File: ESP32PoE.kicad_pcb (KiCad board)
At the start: 4 copper layers, 90 x 40 mm, 56 parts, among them J1 Conn_01x20_Pin, J2 Conn_01x20_Pin, J3 Conn_01x04_Pin, SW1 SW_Push, SW2 SW_Push, U1 W5500, U2 MagJack-A70-112-331N126, U3 AMS1117-3.3, U4 ESP32-S3-WROOM-1, U7 AG9905LP, Y1 XO32F025000GEHE001

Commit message: feat: improve silkscreen
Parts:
- added G***: LOGO, ESP32PoE:Arrow, F.Cu at (156.7, 74.1)
- added G***: LOGO, ESP32PoE:Arrow, B.Cu at (119.3, 69.2)
- moved C15 0.55 mm to (133.2, 88.3)
- moved C11 0.50 mm to (114.5, 81.6)
- moved C16 0.50 mm to (133.4, 90.1)
- moved C20 0.45 mm to (133.2, 91.8)
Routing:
- net Net-(C11-Pad1): track 6.30 -> 6.80 mm
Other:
- board text added: "LAN"
- board text added: "PoE"

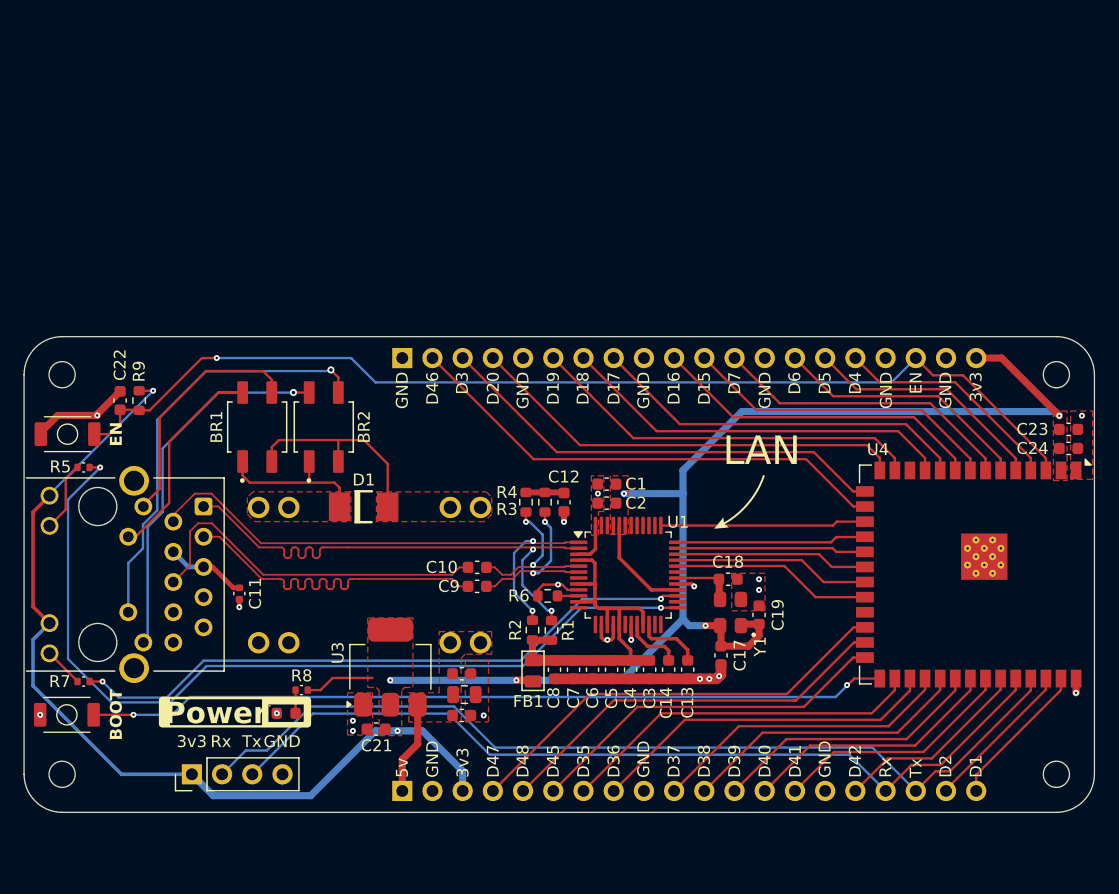
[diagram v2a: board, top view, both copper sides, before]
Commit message: feat: redesign to smaller form factor
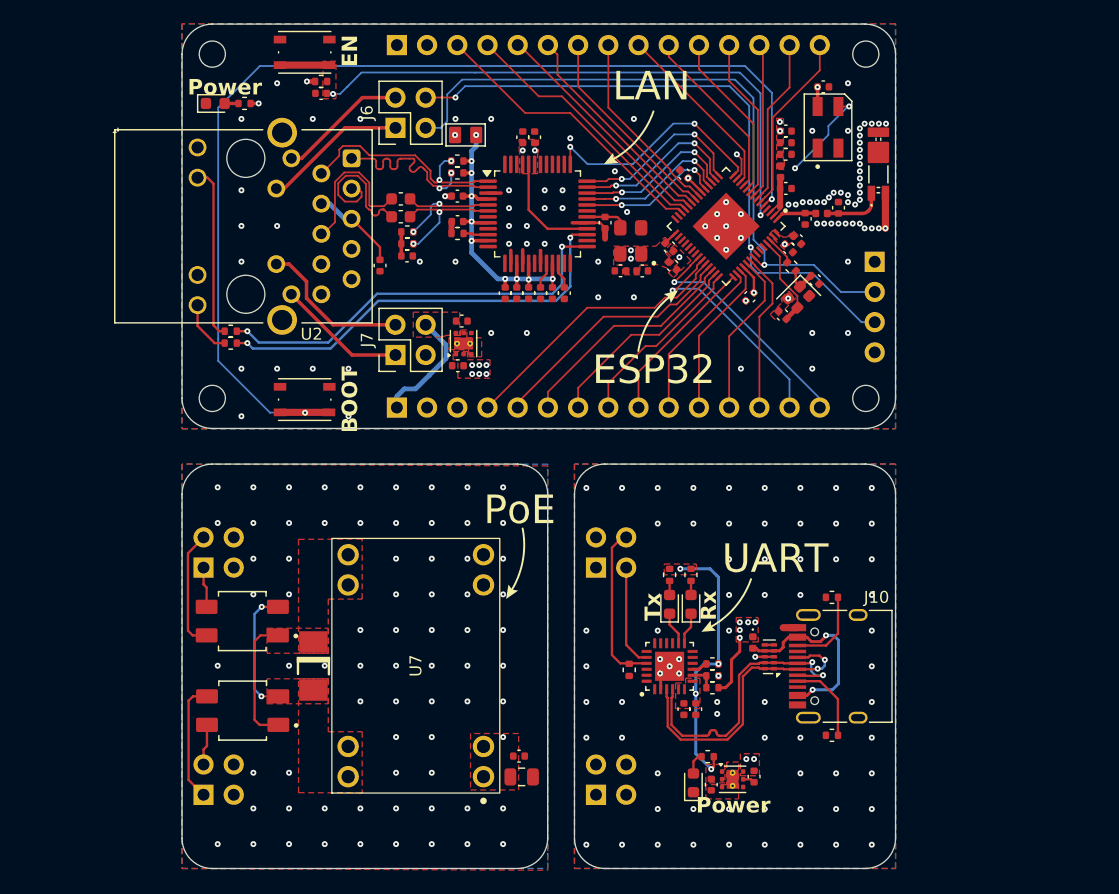
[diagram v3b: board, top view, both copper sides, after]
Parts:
- added AE1: Ant_RFECA3216060A1T_1206, Hardware Components:Ant_RFECA3216060A1T, F.Cu at (168.3, 46.3)
- added C25: 2p7, Hardware Components:C_0402_1005Metric, F.Cu at (162.1, 50.1)
- added C26: 2p4, Hardware Components:C_0402_1005Metric, F.Cu at (164.9, 49.2)
- added C27: 100n, Hardware Components:C_0402_1005Metric, F.Cu at (160.5, 44.7)
- added C28: 100n, Hardware Components:C_0402_1005Metric, F.Cu at (160.5, 47.5)
- added C29: 100n, Hardware Components:C_0402_1005Metric, F.Cu at (151.9, 46.3)
- added C30: 100n, Hardware Components:C_0402_1005Metric, F.Cu at (157.4, 56.6)
- added C31: 1u, Hardware Components:C_0402_1005Metric, F.Cu at (160.5, 43.7)
- added C32: 10u, Hardware Components:C_0402_1005Metric, F.Cu at (160.5, 42.7)
- added C33: 100n, Hardware Components:C_0402_1005Metric, F.Cu at (160.7, 52.6)
- added C34: 1u, Hardware Components:C_0402_1005Metric, F.Cu at (161.4, 51.9)
- added C35: 1u, Hardware Components:C_0402_1005Metric, F.Cu at (150.9, 54.0)
- added C36: 100n, Hardware Components:C_0402_1005Metric, F.Cu at (150.7, 52.5)
- added C37: 100n, Hardware Components:C_0402_1005Metric, F.Cu at (152.9, 91.3)
- added C38: 4u7, Hardware Components:C_0402_1005Metric, F.Cu at (151.9, 91.3)
- added C39: 1u, Hardware Components:C_0402_1005Metric, F.Cu at (157.8, 97.0)
- added C40: 1u, Hardware Components:C_0402_1005Metric, F.Cu at (154.2, 97.7)
- added C41: 100n, Hardware Components:C_0402_1005Metric, F.Cu at (163.6, 39.0)
- added D2: LED, Hardware Components:LED_0603_1608Metric, F.Cu at (152.7, 97.5)
- added D4: D_Schottky_Small, Hardware Components:D_0402_1005Metric, F.Cu at (157.7, 85.7)
- added D5: LED, Hardware Components:LED_0603_1608Metric, F.Cu at (150.7, 82.5)
- added D6: LED, Hardware Components:LED_0603_1608Metric, F.Cu at (152.5, 82.5)
- added D7: SK6812MINI, Hardware Components:LED_SK6812MINI, F.Cu at (164.0, 42.4)
- added G***: LOGO, ESP32PoE:Arrow, F.Cu at (155.6, 82.8)
- added G***: LOGO, ESP32PoE:Arrow, F.Cu at (149.6, 58.5)
- added J10: USB_C_Receptacle_USB2.0_16P, Hardware Components:USB_C_Receptacle_HRO_TYPE-C-31-M-12, F.Cu at (165.5, 87.7)
- added J4: Conn_02x02_Counter_Clockwise, Connector_PinSocket_2.54mm:PinSocket_2x02_P2.54mm_Vertical, B.Cu at (111.5, 79.4)
- added J5: Conn_02x02_Counter_Clockwise, Connector_PinSocket_2.54mm:PinSocket_2x02_P2.54mm_Vertical, B.Cu at (111.5, 98.5)
- added J6: Conn_02x02_Counter_Clockwise, Hardware Components:Conn_PinHeader_2x02_P2.54mm_Vertical, F.Cu at (127.6, 42.4)
- added J7: Conn_02x02_Counter_Clockwise, Hardware Components:Conn_PinHeader_2x02_P2.54mm_Vertical, F.Cu at (127.6, 61.5)
- added J8: Conn_02x02_Counter_Clockwise, Connector_PinSocket_2.54mm:PinSocket_2x02_P2.54mm_Vertical, B.Cu at (144.5, 79.4)
- added J9: Conn_02x02_Counter_Clockwise, Connector_PinSocket_2.54mm:PinSocket_2x02_P2.54mm_Vertical, B.Cu at (144.5, 98.5)
- added L1: 2.4nH, Hardware Components:L_0402_1005Metric, F.Cu at (163.5, 49.6)
- added L2: 2u, Hardware Components:L_0402_1005Metric, F.Cu at (160.0, 46.1)
- added R10: 22, Hardware Components:R_0402_1005Metric, F.Cu at (160.9, 54.1)
- added R11: 1k, Hardware Components:R_0402_1005Metric, F.Cu at (150.7, 80.0)
- added R12: 10k, Hardware Components:R_0402_1005Metric, F.Cu at (147.3, 88.0)
- added R13: 5k1, Hardware Components:R_0402_1005Metric, F.Cu at (164.3, 93.5)
- added R14: 5k1, Hardware Components:R_0402_1005Metric, F.Cu at (164.3, 81.9)
- added R15: 1k, Hardware Components:R_0402_1005Metric, F.Cu at (154.3, 87.5)
- added R16: 22k1, Hardware Components:R_0402_1005Metric, F.Cu at (154.3, 89.5)
- added R17: 47k5, Hardware Components:R_0402_1005Metric, F.Cu at (154.3, 88.5)
- added R18: 1k, Hardware Components:R_0402_1005Metric, F.Cu at (152.5, 80.0)
- added R19: 1k, Hardware Components:R_0402_1005Metric, F.Cu at (153.9, 95.3)
- added U13: TPD4EUSB30, Hardware Components:TPD4EUSB30_USON-10, F.Cu at (159.1, 86.9)
- added U5: ESP32-S3FN8, Hardware Components:MCU_ESP32-S3FN8, F.Cu at (155.4, 50.7)
- added U6: CP2102N-A02-GQFN24R, Hardware Components:CP2102-A02-GQ-QFN-50P, F.Cu at (150.7, 87.7)
- added Y2: ECS-400-10-37B2-CKM-TR, Hardware Components:Oscillator_ECS_400-10-37B2-CKM-TR, F.Cu at (161.5, 56.7)
- BR1, BR2: footprint ESP32PoE:CDBHM1100L-G -> Hardware Components:MB110S
- C1, C13, C14, C15, C17, C18, C19, C2, C22, C3, C4, C5, C6, C7, C8: footprint Capacitor_SMD:C_0603_1608Metric -> Hardware Components:C_0402_1005Metric
- C10, C9: footprint Capacitor_SMD:C_0603_1608Metric -> Hardware Components:C_0603_1608Metric
- C11: footprint Capacitor_SMD:C_0402_1005Metric -> Hardware Components:C_0402_1005Metric
- C12: value 22n -> 10n; footprint Capacitor_SMD:C_0603_1608Metric -> Hardware Components:C_0402_1005Metric
- C16: footprint Capacitor_SMD:C_0805_2012Metric -> Hardware Components:C_0805_2012Metric
- C20, C21: value 22u -> 1u; footprint Capacitor_SMD:C_0603_1608Metric -> Hardware Components:C_0402_1005Metric
- C23: value 10u -> 12pF; footprint Capacitor_SMD:C_0603_1608Metric -> Hardware Components:C_0402_1005Metric
- C24: value 100n -> 12pF; footprint Capacitor_SMD:C_0603_1608Metric -> Hardware Components:C_0402_1005Metric
- D1: footprint ESP32PoE:SMAJ58A -> Hardware Components:D_SMAJ58A
- D3: footprint LED_SMD:LED_0603_1608Metric -> Hardware Components:LED_0603_1608Metric
- G***: moved to F.Cu
- J1, J2: value Conn_01x20_Pin -> Conn_01x15_Pin; footprint Connector_PinHeader_2.54mm:PinHeader_1x20_P2.54mm_Vertical -> Connector_PinHeader_2.54mm:PinHeader_1x15_P2.54mm_Vertical
- J3: moved to B.Cu
- R1, R2, R3, R4, R6, R9: footprint Resistor_SMD:R_0603_1608Metric -> Hardware Components:R_0402_1005Metric
- R5, R7, R8: footprint Resistor_SMD:R_0402_1005Metric -> Hardware Components:R_0402_1005Metric
- SW1, SW2: footprint ESP32PoE:SMD,3x4mm -> Hardware Components:SW_PTS815SJM250SMTRLFS
- U1: footprint Package_QFP:LQFP-48_7x7mm_P0.5mm -> Hardware Components:LQFP-48_7x7mm_P0.5mm
- U2: footprint ESP32PoE:TRJG0926HENL -> Hardware Components:RJ45_USAKRO_DGUK111Q334AB2A2DP057
- U3: value AMS1117-3.3 -> TLV76733DRVx; footprint Package_TO_SOT_SMD:SOT-223-3_TabPin2 -> Hardware Components:WSON-6-1EP_2x2mm_P0.65mm_EP1x1.6mm_ThermalVias
- U4: value ESP32-S3-WROOM-1 -> TLV76733DRVx; footprint RF_Module:ESP32-S3-WROOM-1 -> Hardware Components:WSON-6-1EP_2x2mm_P0.65mm_EP1x1.6mm_ThermalVias
- U7: footprint ESP32PoE:AG9905LP -> Hardware Components:POE_AG9905LP; moved to F.Cu
- Y1: footprint ESP32PoE:SMD3225-4P -> Hardware Components:Oscillator_TDK_SMD3225-4P
- moved J3 71.8 mm to (167.9, 53.7), turned to 180 degrees
- moved H4 62.6 mm to (167.2, 36.2), turned to 90 degrees
- moved H2 61.9 mm to (112.2, 36.2)
- moved SS3 51.7 mm to (164.2, 42.6)
- moved D3 51.6 mm to (112.5, 40.4)
- moved U4 50.2 mm to (133.4, 60.6), turned to 90 degrees
- moved R8 49.6 mm to (114.9, 40.4)
- moved FB1 45.4 mm to (133.5, 43.0), turned to 0 degrees
- moved C7 41.0 mm to (132.8, 48.2), turned to 180 degrees
- moved R2 39.9 mm to (132.8, 45.2), turned to 180 degrees
- moved C6 39.3 mm to (132.8, 50.3), turned to 180 degrees
- moved R1 39.3 mm to (132.8, 46.2), turned to 180 degrees
- moved SW1 37.8 mm to (120.0, 36.1)
- moved G*** 33.7 mm to (156.5, 50.7)
- moved C14 33.4 mm to (139.8, 56.3)
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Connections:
- BR1 pad 3: /LAN/VINA -> /PoE/VINB
- BR1 pad 4: /LAN/VINB -> /PoE/VINA
- BR2 pad 3: /LAN/VINC -> /PoE/VIND
- BR2 pad 4: /LAN/VIND -> /PoE/VINC
- C15 pad 1: GND -> GND_PoE
- C15 pad 2: +5V -> +5V_PoE
- C16 pad 1: +5V -> +5V_PoE
- C16 pad 2: GND -> GND_PoE
- C22 pad 1: /ESP/EN -> /MCU/EN
- C23 pad 1: +3.3V -> Net-(C23-Pad1)
- C24 pad 1: +3.3V -> /MCU/XTAL_N
- J1 pad 10: /ESP/IO37 -> /MCU/IO39
- J1 pad 11: /ESP/IO38 -> /MCU/IO40
- J1 pad 12: /ESP/IO39 -> /MCU/IO41
- J1 pad 13: /ESP/IO40 -> /MCU/IO42
- J1 pad 14: /ESP/IO41 -> /MCU/IO47
- J1 pad 15: GND -> /MCU/IO48
- J1 pad 4: /ESP/IO47 -> /MCU/IO33
- J1 pad 5: /ESP/IO48 -> /MCU/IO34
- J1 pad 6: /ESP/IO45 -> /MCU/IO35
- J1 pad 7: /ESP/IO35 -> /MCU/IO36
- J1 pad 8: /ESP/IO36 -> /MCU/IO37
- J1 pad 9: GND -> /MCU/IO38
- J2 pad 1: GND -> +3.3V
- J2 pad 10: /ESP/IO16 -> /MCU/IO6
- J2 pad 11: /ESP/IO15 -> /MCU/IO5
- J2 pad 12: /ESP/IO7 -> /MCU/IO4
- J2 pad 13: GND -> /MCU/IO3
- J2 pad 14: /ESP/IO6 -> /MCU/IO2
- J2 pad 15: /ESP/IO5 -> /MCU/IO1
- J2 pad 2: /ESP/IO46 -> GND
- J2 pad 3: /ESP/IO3 -> /MCU/IO20
- J2 pad 4: /ESP/IO20 -> /MCU/IO19
- J2 pad 5: GND -> /MCU/IO18
- J2 pad 6: /ESP/IO19 -> /MCU/IO17
- J2 pad 7: /ESP/IO18 -> /MCU/IO16
- J2 pad 8: /ESP/IO17 -> /MCU/IO15
- J2 pad 9: GND -> /MCU/IO7
- J3 pad 2: /ESP/TX -> TX
- J3 pad 3: /ESP/RX -> RX
- R9 pad 2: /ESP/EN -> /MCU/EN
- SW1 pad 2: /ESP/EN -> /MCU/EN
- SW2 pad 2: /ESP/BOOT_OPT -> /MCU/BOOT_OPT
- U1 pad 32: /ESP/LAN.~{SCS} -> /LAN/LAN.~{SCS}
- U1 pad 33: /ESP/LAN.SCLK -> /LAN/LAN.SCLK
- U1 pad 34: /ESP/LAN.MISO -> /LAN/LAN.MISO
- U1 pad 35: /ESP/LAN.MOSI -> /LAN/LAN.MOSI
- U1 pad 36: /ESP/LAN.~{INT} -> /LAN/LAN.~{INT}
- U1 pad 37: /ESP/LAN.~{RST} -> /LAN/LAN.~{RST}
- U3 pad 1: GND -> +3.3V_USB
- U3 pad 2: +3.3V -> +3.3V_USB
- U3 pad 3: +5V -> GND_USB
- U4 pad 1: GND -> +3.3V
- U4 pad 3: /ESP/EN -> GND
- U4 pad 4: /ESP/IO4 -> unconnected-(U4-EN-Pad4)
- U4 pad 5: /ESP/IO5 -> GND
- U4 pad 6: /ESP/IO6 -> +5V
- U4 pad 7: /ESP/IO7 -> GND
- U7 pad 1: +5V -> +5V_PoE
- U7 pad 2: GND -> GND_PoE
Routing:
- net +3.3V: track 191.1 -> 17.9 mm, vias 7 -> 19
- net /MCU/BOOT_OPT: track 0.00 -> 93.3 mm, vias 0 -> 2
- net /ESP/EN: track 89.5 -> 0.00 mm, vias 1 -> 0
- net /ESP/TX: track 77.8 -> 0.00 mm
- net /ESP/RX: track 73.5 -> 0.00 mm
- net /ESP/BOOT_OPT: track 67.4 -> 0.00 mm, vias 2 -> 0
- net TX: track 0.00 -> 57.0 mm, vias 0 -> 1
- net RX: track 0.00 -> 55.0 mm, vias 0 -> 2
- net /MCU/EN: track 0.00 -> 52.7 mm, vias 0 -> 2
- net /ESP/IO46: track 41.5 -> 0.00 mm
- net /LAN/ETH.LEDG: track 74.2 -> 35.0 mm
- net /ESP/IO3: track 38.5 -> 0.00 mm
- net /ESP/IO20: track 37.1 -> 0.00 mm
- net /ESP/IO47: track 37.0 -> 0.00 mm
- net /ESP/IO48: track 33.9 -> 0.00 mm
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- added copper zone on In2.Cu, net +3.3V
- added copper zone on F.Cu, net +3.3V_USB
- added copper zone on B.Cu, net +5V_PoE
- added copper zone on F.Cu, net +5V_PoE
- added copper zone on F.Cu, net +5V_USB
- added copper zone on In2.Cu, net +5V_USB
- added copper zone on F.Cu, net /MCU/EN
- added copper zone on F.Cu, net /MCU/RF_ANT
- added copper zone on B.Cu, net GND
- added copper zone on F.Cu, net GND_PoE
- added copper zone on In1.Cu, net GND_PoE
- added copper zone on In2.Cu, net GND_PoE
- added copper zone on B.Cu, net GND_USB
- added copper zone on F.Cu, net GND_USB
- added copper zone on In1.Cu, net GND_USB
- removed copper zone on In2.Cu, net GND
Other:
- board size 90 x 40 mm -> 60 x 71 mm
- board text added: "15"
- board text added: "16"
- board text added: "17"
- board text added: "18"
- board text added: "19"
- board text added: "2"
- board text added: "20"
- board text added: "3"
- board text added: "33"
- board text added: "34"
- board text added: "35"
- board text added: "36"
- board text added: "37"
- board text added: "38"
- board text added: "39"
- board text added: "40"
- board text added: "41"
- board text added: "42"
- board text added: "47"
- board text added: "48"
- board text added: "5"
- board text added: "6"
- board text added: "7"
- board text added: "ESP32"
- board text added: "UART"
- board text added: "V0.2"
- board text removed: "D1"
- board text removed: "D15"
- board text removed: "D16"
- board text removed: "D17"
- board text removed: "D18"
- board text removed: "D19"
- board text removed: "D2"
- board text removed: "D20"
- board text removed: "D3"
- board text removed: "D35"
- board text removed: "D36"
- board text removed: "D37"
- board text removed: "D38"
- board text removed: "D39"
- board text removed: "D4"
- board text removed: "D40"
- board text removed: "D41"
- board text removed: "D42"
- board text removed: "D45"
- board text removed: "D46"
- board text removed: "D47"
- board text removed: "D48"
- board text removed: "D5"
- board text removed: "D6"
- board text removed: "D7"
- board text removed: "ESP32 PoE"
- board text removed: "v0.1"

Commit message: wip: mini form factor
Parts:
- FB1: footprint ESP32PoE:L0805 -> Hardware Components:FB_0805_2012Metric
- moved C21 0.75 mm to (133.6, 62.4), turned to 0 degrees
- moved C20 0.33 mm to (132.9, 58.7)
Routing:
- net +3.3V: vias 19 -> 17
